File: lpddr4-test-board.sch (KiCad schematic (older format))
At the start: 0 parts

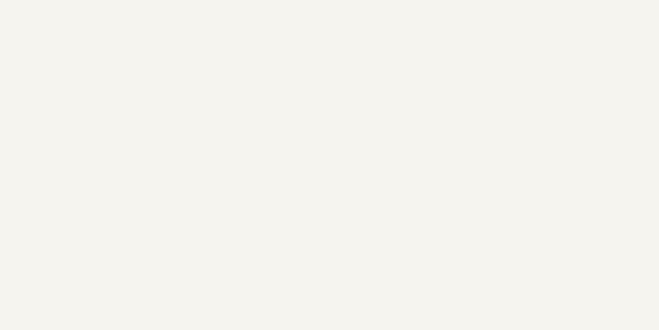
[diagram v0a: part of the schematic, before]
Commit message: Update block diagram
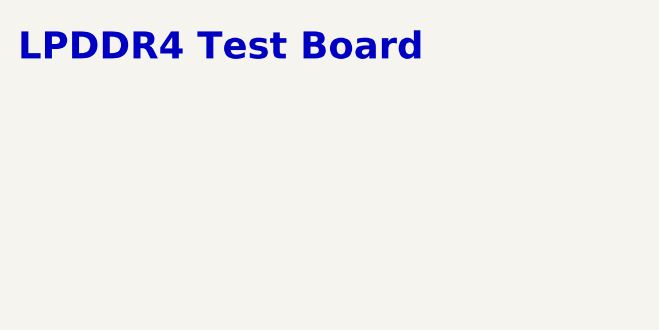
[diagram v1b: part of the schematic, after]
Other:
- note added: "LPDDR4 Test Board"
